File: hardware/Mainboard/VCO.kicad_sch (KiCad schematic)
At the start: 26 parts, among them J15 Jumper, J16 Jumper, J17 Jumper, Q11 2N3904, Q12 2N3904, Q14 2N3904, SW1 SW_SPDT, U2 TL074, U4 TL074

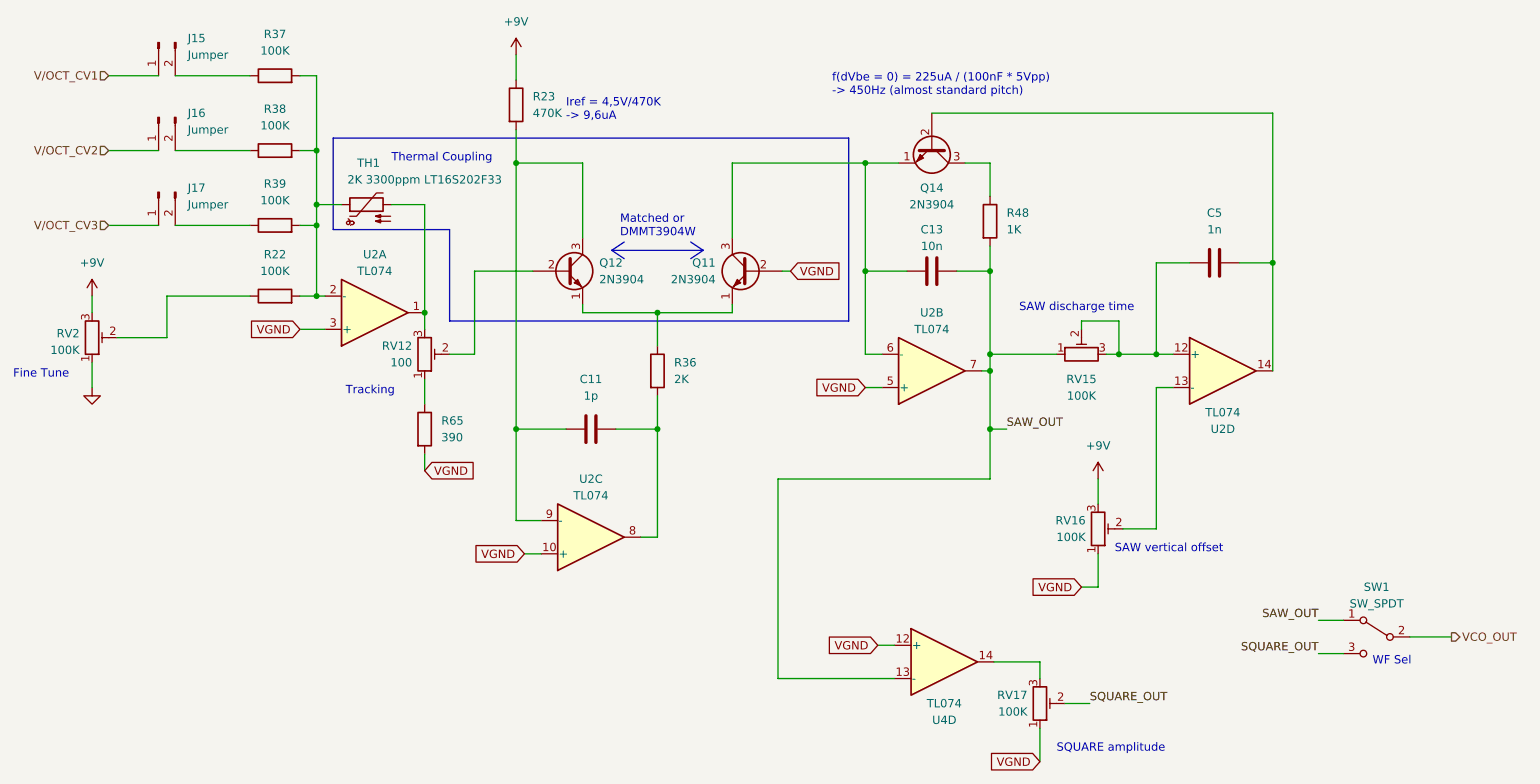
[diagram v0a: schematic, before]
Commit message: add 0v2 status
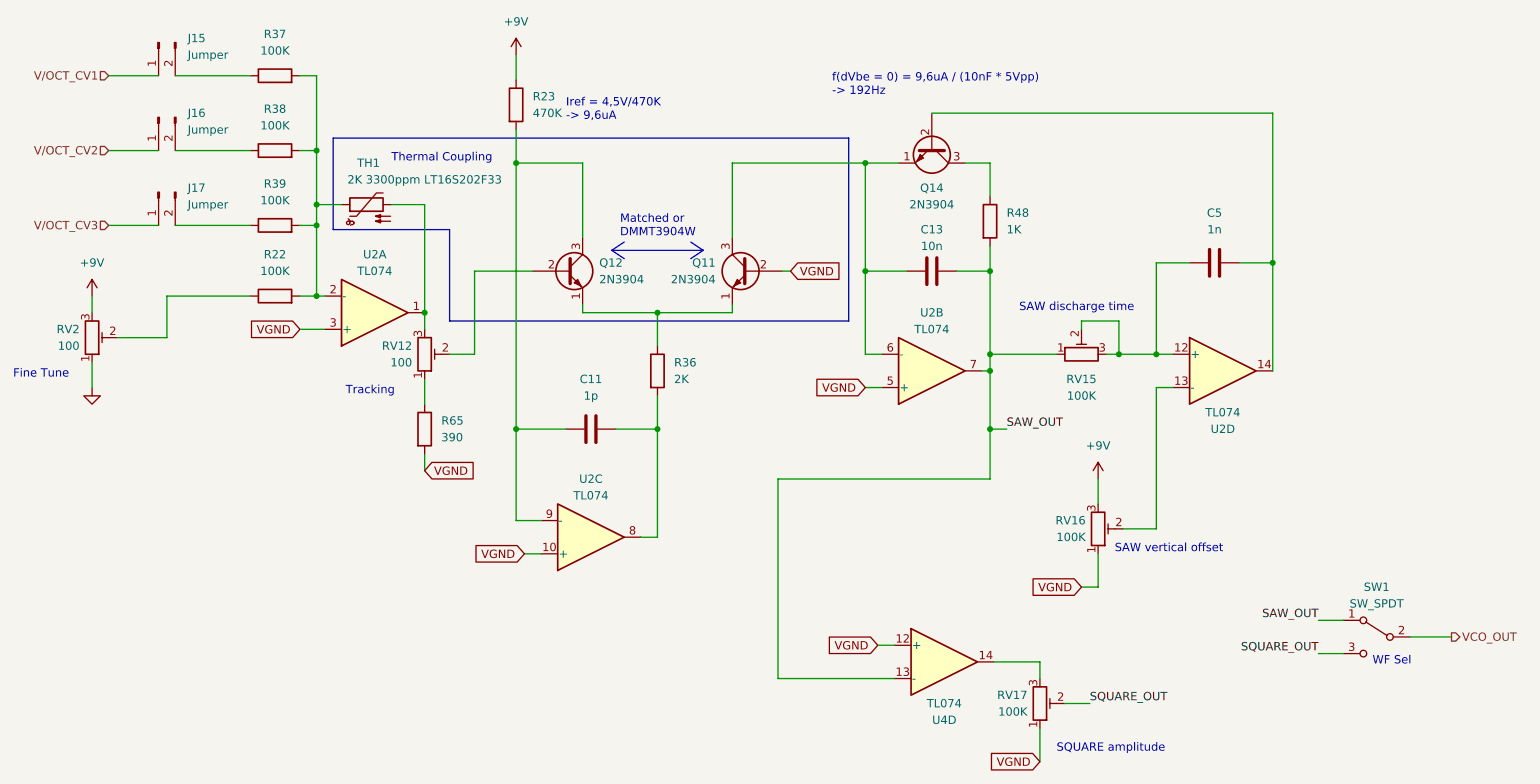
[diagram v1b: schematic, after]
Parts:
- RV2: value 100K -> 100
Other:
- note added: "f(dVbe = 0) = 9,6uA / (10nF * 5Vpp) -> 192Hz"
- note removed: "f(dVbe = 0) = 225uA / (100nF * 5Vpp) -> 450Hz (almost standard pitch)"
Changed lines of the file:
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@@
     (stroke (width 0) (type default))
   )
-  (text "f(dVbe = 0) = 225uA / (100nF * 5Vpp)\n-> 450Hz (almost standard pitch)"
-    (at 158.115 43.18 0)
+  (text "f(dVbe = 0) = 9,6uA / (10nF * 5Vpp)\n-> 192Hz" (at 158.115 43.18 0)
     (effects (font (size 1.27 1.27)) (justify left bottom))
   )
@@
   (symbol (lib_id "Device:R_Potentiometer_Trim") (at 45.085 80.01 0) (mirror x) (unit 1)
     (in_bom yes) (on_board yes) (dnp no) (fields_autoplaced)
-    (property "Reference" "RV2" (at 43.18 79.375 0)
-      (effects (font (size 1.27 1.27)) (justify right))
-    )
-    (property "Value" "100K" (at 43.18 81.915 0)
-      (effects (font (size 1.27 1.27)) (justify right))
-    )
+    (property "Reference" "RV2" (at 43.18 78.7399 0)
+      (effects (font (size 1.27 1.27)) (justify right))
+    )
+    (property "Value" "100" (at 43.18 81.2799 0)
+      (effects (font (size 1.27 1.27)) (justify right))
+    )

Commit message: Backport from 0v3
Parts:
- RV2: value 100 -> 100K
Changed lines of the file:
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@@
     (effects (font (size 1.27 1.27)) (justify left bottom))
   )
-  (text "Iref = 4,5V/470K\n-> 9,6uA" (at 117.475 46.99 0)
+  (text "Iref = 4,5V/470K\n-> 9,6uA" (at 119.38 46.355 0)
     (effects (font (size 1.27 1.27)) (justify left bottom))
   )
@@
       (effects (font (size 1.27 1.27)) (justify right))
     )
-    (property "Value" "100" (at 43.18 81.2799 0)
-      (effects (font (size 1.27 1.27)) (justify right))
-    )
+    (property "Value" "100K" (at 43.18 81.2799 0)
+      (effects (font (size 1.27 1.27)) (justify right))
+    )
